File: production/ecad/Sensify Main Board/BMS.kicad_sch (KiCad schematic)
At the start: 76 parts, among them J1 1-2834011-3, J2 1-2834011-2, Q1 2N700, Q2 PMPB13XNE,115, Q3 PMPB13XNE,115, Q4 BSS223PWH6327XTSA1, SW3 500ASSP3M2QE, U1 MAX17320G22, U2 BQ25306RTER, U3 LD29150DT33R, U4 LM22676MRX-5.0_NOPB

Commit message: changed tp names + attempted to start placing mcu and making space for mounting holes?
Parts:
- renumbered USB_9V+1 to TP12, BAT1+_TP1 to TP13, BAT1-/BAT2+_TP1 to TP14, PACK+_TP1 to TP15, BMS_ALERT_TP1 to TP16, CHG_TP1 to TP17, DIS_TP1 to TP18, TH1_TP1 to TP19, PMID_TP1 to TP20, STAT_TP1 to TP21
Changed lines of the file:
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@@
   (symbol (lib_id "Connector:TestPoint") (at 100.33 90.17 0) (unit 1)
     (in_bom yes) (on_board yes) (dnp no)
-    (property "Reference" "DIS_TP1" (at 101.6 87.63 0)
+    (property "Reference" "TP18" (at 101.6 87.63 0)
       (effects (font (size 1.27 1.27)) (justify left))
     )
@@
       (project "Sensify Main Board"
         (path "/9a7ba7c3-7d28-4a83-bdbc-38fbff59fcbe/13ad10b4-913e-414a-9863-b902179dcb8b"
-          (reference "DIS_TP1") (unit 1)
+          (reference "TP18") (unit 1)
         )
       )
@@
   (symbol (lib_id "Connector:TestPoint") (at 77.47 90.17 0) (mirror y) (unit 1)
     (in_bom yes) (on_board yes) (dnp no)
-    (property "Reference" "CHG_TP1" (at 76.2 87.63 0)
+    (property "Reference" "TP17" (at 76.2 87.63 0)
       (effects (font (size 1.27 1.27)) (justify left))
     )
@@
       (project "Sensify Main Board"
         (path "/9a7ba7c3-7d28-4a83-bdbc-38fbff59fcbe/13ad10b4-913e-414a-9863-b902179dcb8b"
-          (reference "CHG_TP1") (unit 1)
+          (reference "TP17") (unit 1)
         )
       )
@@
   (symbol (lib_id "Connector:TestPoint") (at 151.13 26.67 0) (unit 1)
     (in_bom yes) (on_board yes) (dnp no)
-    (property "Reference" "USB_9V+1" (at 152.4 25.4 0)
+    (property "Reference" "TP12" (at 152.4 25.4 0)
       (effects (font (size 1.27 1.27)) (justify left))
     )
@@
       (project "Sensify Main Board"
         (path "/9a7ba7c3-7d28-4a83-bdbc-38fbff59fcbe/13ad10b4-913e-414a-9863-b902179dcb8b"
-          (reference "USB_9V+1") (unit 1)
+          (reference "TP12") (unit 1)
         )
       )
@@
   (symbol (lib_id "Connector:TestPoint") (at 116.84 186.69 0) (unit 1)
     (in_bom yes) (on_board yes) (dnp no)
-    (property "Reference" "PMID_TP1" (at 106.68 181.61 0)
+    (property "Reference" "TP20" (at 106.68 181.61 0)
       (effects (font (size 1.27 1.27)) (justify left))
     )
@@
       (project "Sensify Main Board"
         (path "/9a7ba7c3-7d28-4a83-bdbc-38fbff59fcbe/13ad10b4-913e-414a-9863-b902179dcb8b"
-          (reference "PMID_TP1") (unit 1)
+          (reference "TP20") (unit 1)
         )
       )
@@
   (symbol (lib_id "Connector:TestPoint") (at 170.18 26.67 0) (unit 1)
     (in_bom yes) (on_board yes) (dnp no)
-    (property "Reference" "PACK+_TP1" (at 171.45 25.4 0)
+    (property "Reference" "TP15" (at 171.45 25.4 0)
       (effects (font (size 1.27 1.27)) (justify left))
     )
@@
       (project "Sensify Main Board"
         (path "/9a7ba7c3-7d28-4a83-bdbc-38fbff59fcbe/13ad10b4-913e-414a-9863-b902179dcb8b"
-          (reference "PACK+_TP1") (unit 1)
+          (reference "TP15") (unit 1)
         )
       )
@@
   (symbol (lib_id "Connector:TestPoint") (at 170.18 40.64 0) (unit 1)
     (in_bom yes) (on_board yes) (dnp no)
-    (property "Reference" "BMS_ALERT_TP1" (at 171.45 39.37 0)
+    (property "Reference" "TP16" (at 171.45 39.37 0)
       (effects (font (size 1.27 1.27)) (justify left))
     )
@@
       (project "Sensify Main Board"
         (path "/9a7ba7c3-7d28-4a83-bdbc-38fbff59fcbe/13ad10b4-913e-414a-9863-b902179dcb8b"
-          (reference "BMS_ALERT_TP1") (unit 1)
+          (reference "TP16") (unit 1)
         )
       )
@@
   (symbol (lib_id "Connector:TestPoint_Small") (at 86.36 200.66 0) (mirror y) (unit 1)
     (in_bom yes) (on_board yes) (dnp no)
-    (property "Reference" "STAT_TP1" (at 85.09 200.66 0)
+    (property "Reference" "TP21" (at 85.09 200.66 0)
       (effects (font (size 1.27 1.27)) (justify left))
     )
@@
       (project "Sensify Main Board"
         (path "/9a7ba7c3-7d28-4a83-bdbc-38fbff59fcbe/13ad10b4-913e-414a-9863-b902179dcb8b"
-          (reference "STAT_TP1") (unit 1)
+          (reference "TP21") (unit 1)
         )
       )
@@
   (symbol (lib_id "Connector:TestPoint") (at 119.38 147.32 0) (unit 1)
     (in_bom yes) (on_board yes) (dnp no)
-    (property "Reference" "TH1_TP1" (at 120.65 144.78 0)
+    (property "Reference" "TP19" (at 120.65 144.78 0)
       (effects (font (size 1.27 1.27)) (justify left))
     )
@@
       (project "Sensify Main Board"
         (path "/9a7ba7c3-7d28-4a83-bdbc-38fbff59fcbe/13ad10b4-913e-414a-9863-b902179dcb8b"
-          (reference "TH1_TP1") (unit 1)
+          (reference "TP19") (unit 1)
         )
       )
@@
   (symbol (lib_id "Connector:TestPoint") (at 151.13 54.61 0) (unit 1)
     (in_bom yes) (on_board yes) (dnp no)
-    (property "Reference" "BAT1-/BAT2+_TP1" (at 152.4 52.07 0)
+    (property "Reference" "TP14" (at 152.4 52.07 0)
       (effects (font (size 1.27 1.27)) (justify left))
     )
@@
       (project "Sensify Main Board"
         (path "/9a7ba7c3-7d28-4a83-bdbc-38fbff59fcbe/13ad10b4-913e-414a-9863-b902179dcb8b"
-          (reference "BAT1-/BAT2+_TP1") (unit 1)
+          (reference "TP14") (unit 1)
         )
       )
@@
   (symbol (lib_id "Connector:TestPoint") (at 151.13 40.64 0) (unit 1)
     (in_bom yes) (on_board yes) (dnp no)
-    (property "Reference" "BAT1+_TP1" (at 152.4 38.1 0)
+    (property "Reference" "TP13" (at 152.4 38.1 0)
       (effects (font (size 1.27 1.27)) (justify left))
     )
@@
       (project "Sensify Main Board"
         (path "/9a7ba7c3-7d28-4a83-bdbc-38fbff59fcbe/13ad10b4-913e-414a-9863-b902179dcb8b"
-          (reference "BAT1+_TP1") (unit 1)
+          (reference "TP13") (unit 1)
         )
       )

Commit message: routing generally done
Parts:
- removed C13: 0.47u, Capacitor_SMD:C_0402_1005Metric_Pad0.74x0.62mm_HandSolder, symbol Device:C
- removed R12, R3: 0, Resistor_SMD:R_0402_1005Metric_Pad0.72x0.64mm_HandSolder, symbol Device:R_US
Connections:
- net GND: now also R2.2
- net at R7.2: now also U1.14 (CSN); no longer U1.15 (CSP)
- net at R7.3: now also U1.15 (CSP); no longer U1.14 (CSN)
- net AOLDO_OUT: no longer names the net of R15.1, U1.12 (AOLDO)
- net AOLDO_OUT: no longer R2.1
- net CHARGER_EN: no longer names the net of U2.6 (~{EN})
- net CHARGER_EN: now also R2.1; no longer R2.2
- no-connect marks 6 -> 7
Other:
- moved on the sheet: R7

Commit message: Added LCSC parts to KiCAD
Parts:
- C1, C8, C9: LCSC (none) -> C92361
- C10: LCSC (none) -> C15850
- C11, C4, C5: LCSC (none) -> C1524
- C12: LCSC (none) -> C82219
- C13: renamed from C14; LCSC (none) -> C26412
- C14: renamed from C15; LCSC (none) -> C15850
- C15: renamed from C16; LCSC (none) -> C14790
- C16: renamed from C19; LCSC (none) -> C15850
- C17: LCSC (none) -> C110037
- C18: LCSC (none) -> C15849
- C19: renamed from C20; LCSC (none) -> C7248
- C2, C7: LCSC (none) -> C1581
- C20: renamed from C21; LCSC (none) -> C1953001
- C21: renamed from C22; LCSC (none) -> C15849
- C22: renamed from C23; LCSC (none) -> C15849
- C3: LCSC (none) -> C43922
- C6: LCSC (none) -> C72203
- D1: LCSC (none) -> C125093
- D2: LCSC (none) -> C6150013
- D3: LCSC (none) -> C106867
- F1: LCSC (none) -> C3672263
- L1: LCSC (none) -> C3222957
- L2: LCSC (none) -> C360734
- Q2, Q3: LCSC (none) -> C553019
- U1: LCSC (none) -> C2914309
- U2: LCSC (none) -> C3682611
- U3: LCSC (none) -> C155674
- U4: LCSC (none) -> C485622
- renumbered R11 to R10, R13 to R11, R14 to R12, R15 to R13, R16 to R14, R17 to R15, R18 to R16, R19 to R17, R20 to R18, R21 to R19, R4 to R2, R22 to R20, R23 to R21, R24 to R22, R5 to R3, R6 to R4, R7 to R5, R8 to R6, R2 to R7, R9 to R8, R10 to R9, SW3 to SW1, TP19 to TP10, TP12 to TP11, TP13 to TP12, TP14 to TP13, TP15 to TP14, TP16 to TP15, TP17 to TP6, TP21 to TP7, TP18 to TP8, TP20 to TP9

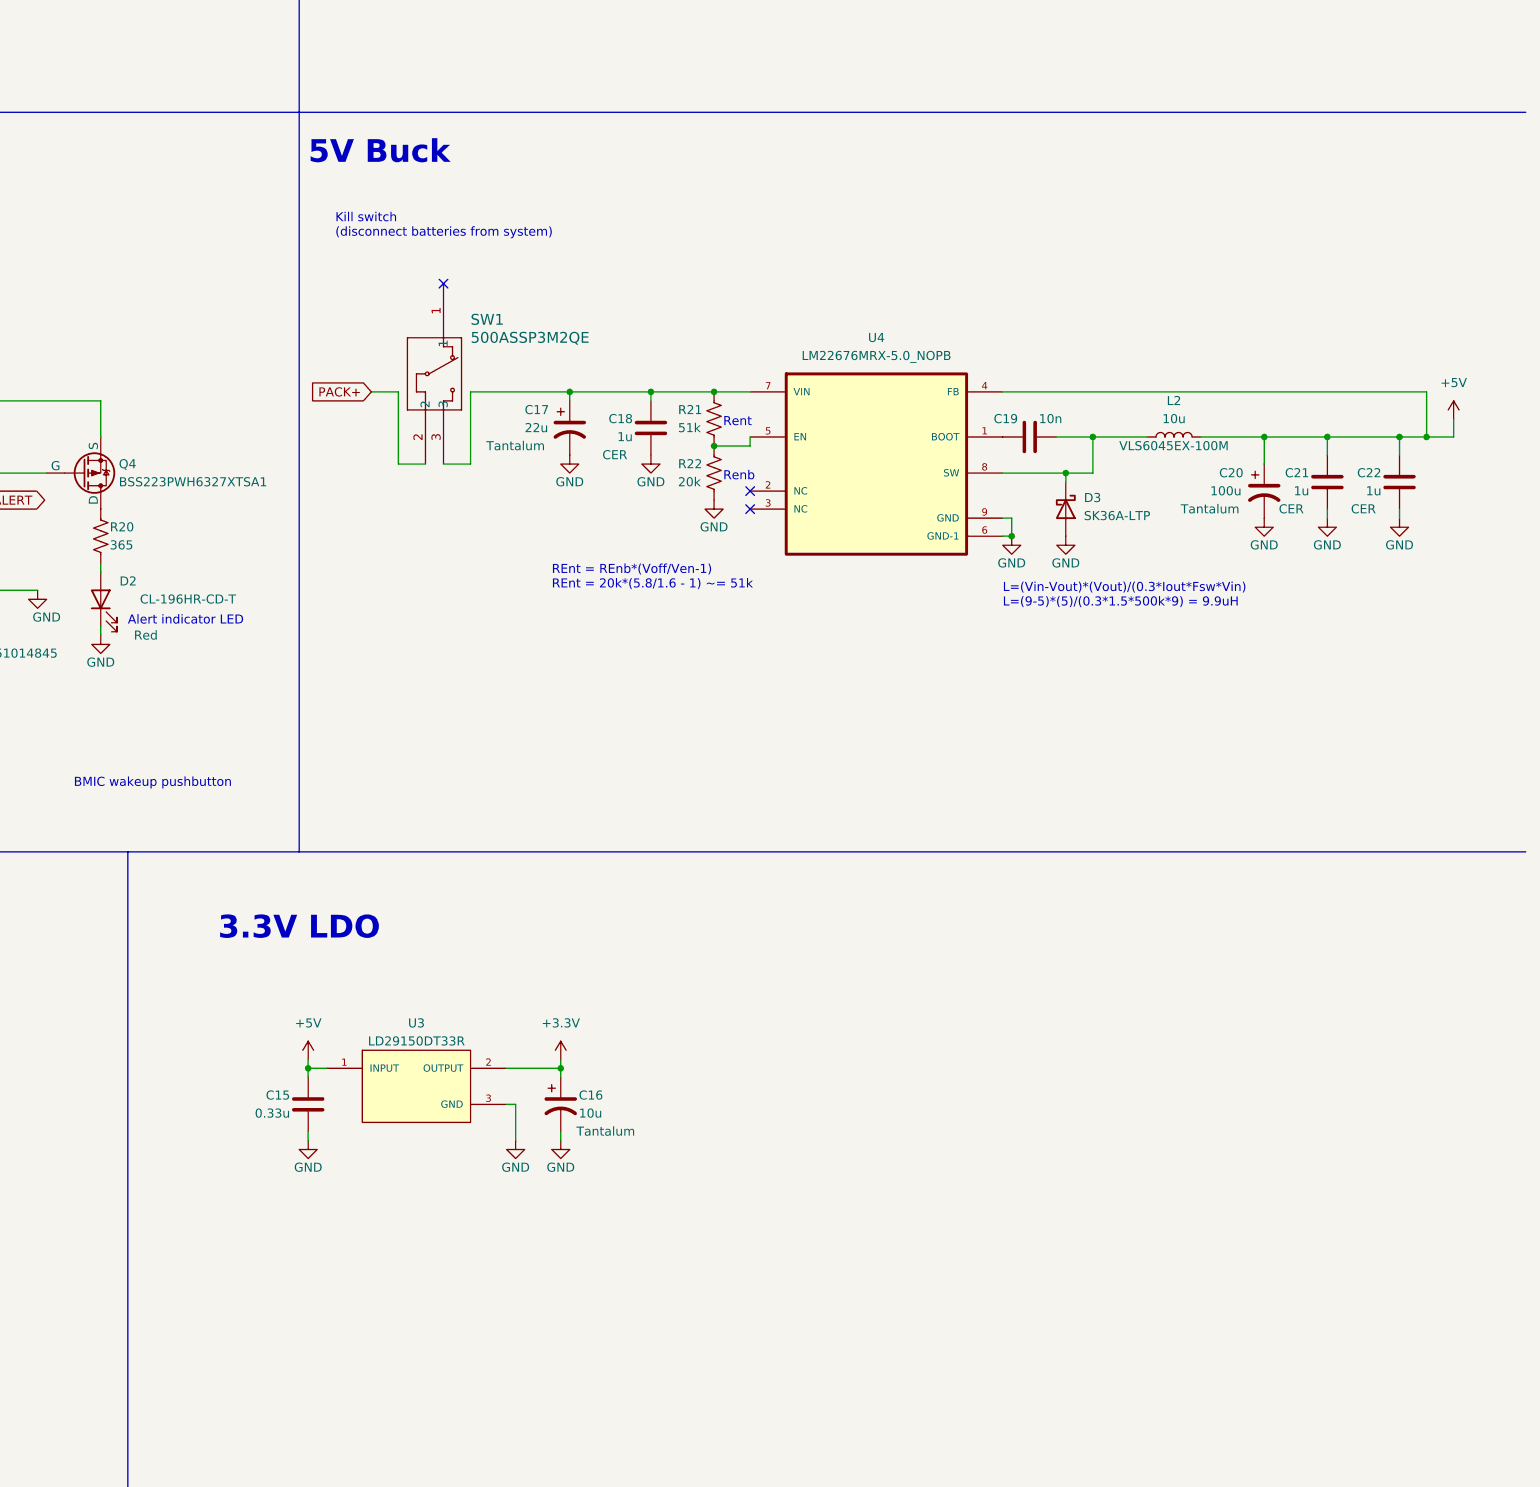
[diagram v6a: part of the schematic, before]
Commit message: added mosfet for load switch to bms + adjusted layout accordingly + fixed outdated ref degs
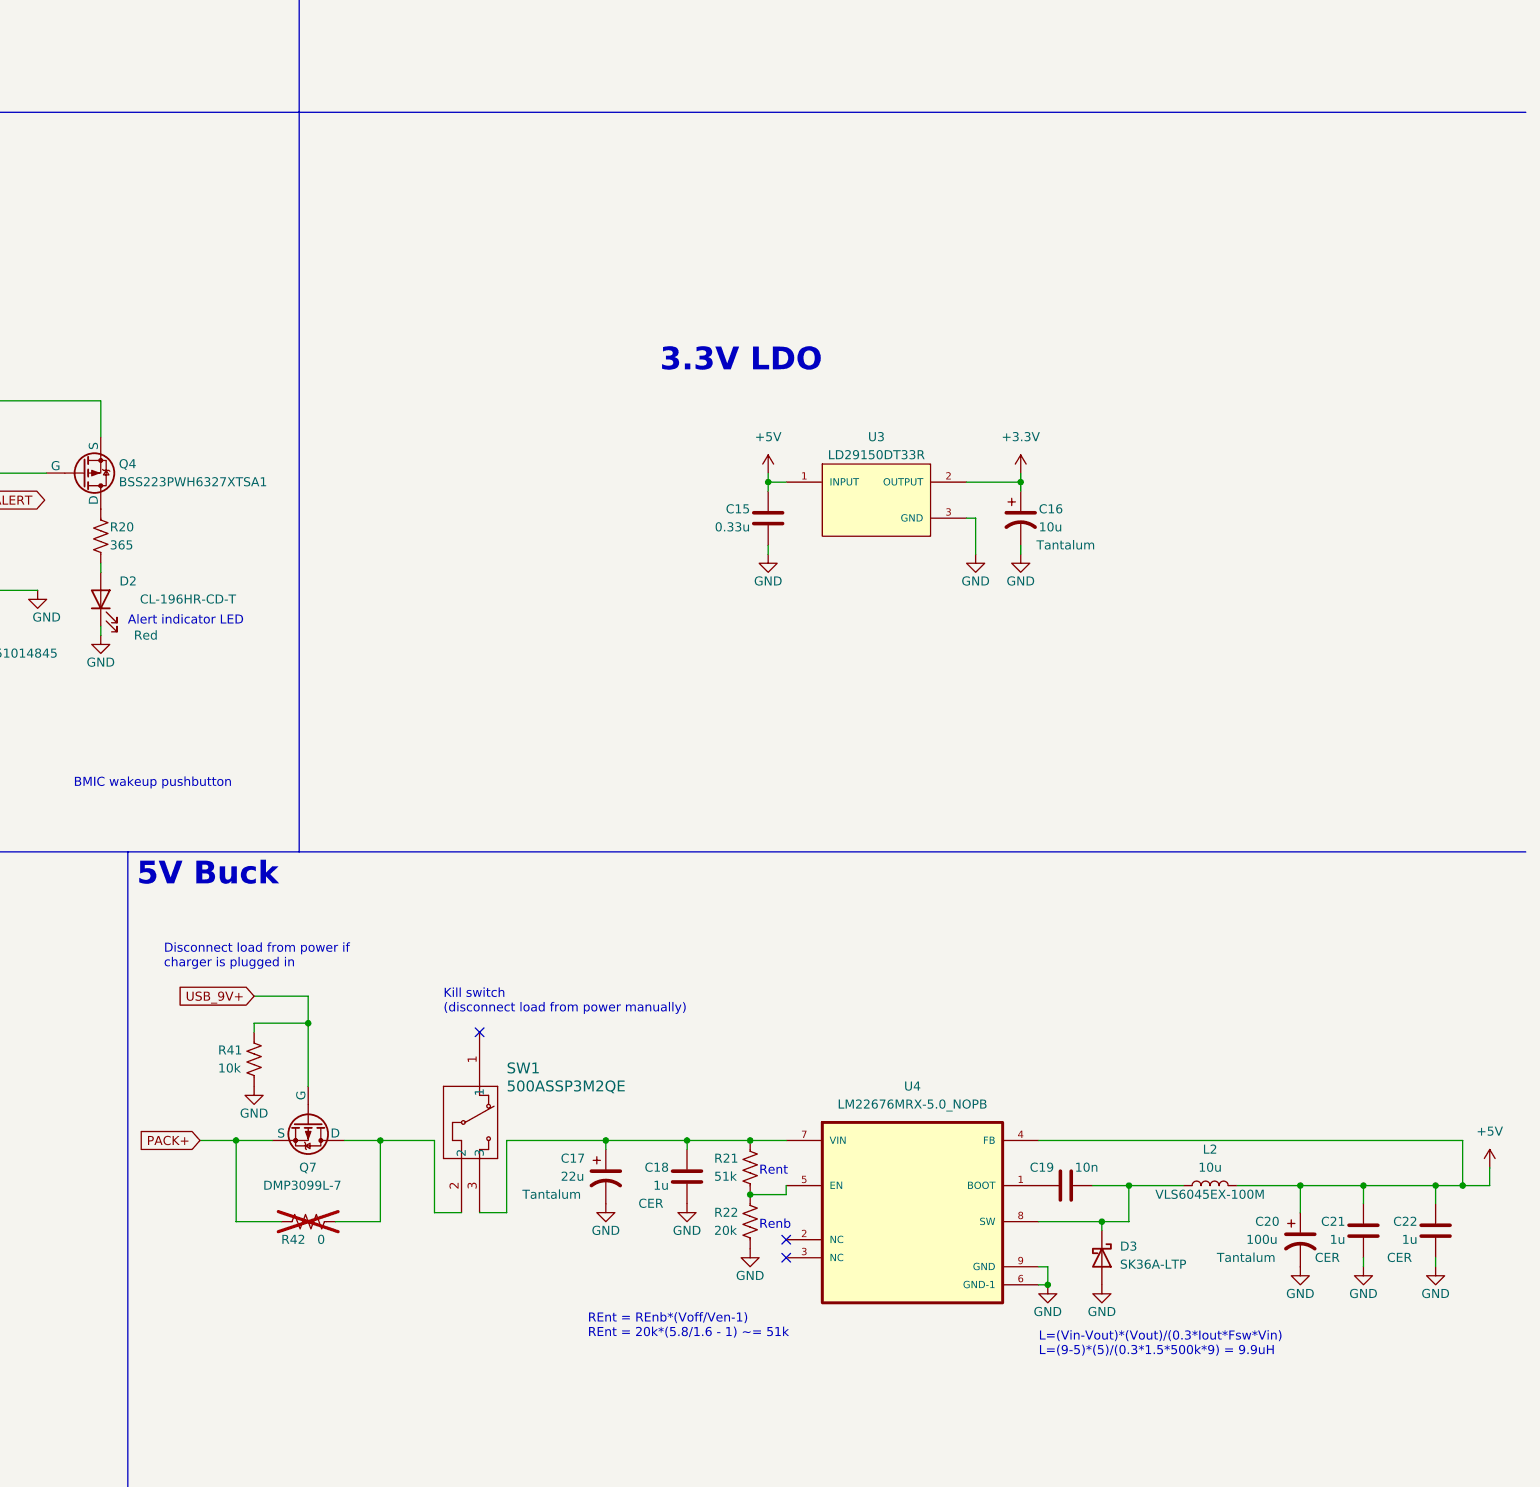
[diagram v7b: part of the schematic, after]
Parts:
- added Q7: DMP3099L-7, Sensify Footprints:DMP3099L-7_DIO, symbol Simulation_SPICE:PMOS
- added R41: 10k, Resistor_SMD:R_0402_1005Metric, symbol Device:R_US
- added R42: 0, Resistor_SMD:R_0402_1005Metric_Pad0.72x0.64mm_HandSolder, symbol Device:R_US
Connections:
- net GND: now also R41.2
- net PACK+: now also Q7.3 (S), R42.2; no longer SW1.2
- net USB_9V+: now also Q7.2 (G), R41.1
- new net: Q7.1 (D), R42.1, SW1.2
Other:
- note added: "Disconnect load from power if charger is plugged in"
- note added: "Kill switch (disconnect load from power manually)"
- note removed: "Kill switch (disconnect batteries from system)"
- moved on the sheet: C15, C16, C17, C18, C19, C20, C21, C22, D3, L2, R21, R22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
